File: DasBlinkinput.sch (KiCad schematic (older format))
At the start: 11 parts, among them P101 CONN_01X02, P102 CONN_01X01, P103 CONN_01X01, P104 CONN_01X05, U101 LP2980

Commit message: revised feedback resistor and updated reference voltage divider
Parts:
- removed R102: 10K, Resistors_SMD:R_0805_HandSoldering, symbol R_Small
- R102: renamed from R103; value 10K -> 5K
- RV101: value POT -> 10K; Fieldname (none) -> Value
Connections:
- net Channel1Photodetect/REF_V: now also RV101.2; no longer RV101.3
- net GND: now also RV101.1
- net at R102.1: now also RV101.3; no longer RV101.2
- no-connect marks 1 -> 0
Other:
- note added: "Note 1: Sense resistors sized for 2V @ 1uA\nNote 2: Minimum ESR required for C102\nNote 3: Input voltage is +5V\nNote 4: Reference voltage varies from 0V to +2V"
- note removed: "Note 1: Check the sense resistors\nNote 2: Spec the tantalum cap\nNote 3: Size the pot\nNote 4: Check diode current and resistor sizing"
- moved on the sheet: R102
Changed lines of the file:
@@
 $EndComp
 $Comp
-L R_Small R103
+L R_Small R102
 U 1 1 582376EF
-P 4770 4450
-F 0 "R103" V 4850 4410 50  0000 L CNN
-F 1 "10K" V 4700 4330 50  0000 L CNN
-F 2 "Resistors_SMD:R_0805_HandSoldering" H 4770 4450 50  0001 C CNN
-F 3 "" H 4770 4450 50  0000 C CNN
-F 4 "Value" H 4770 4450 60  0001 C CNN "Fieldname"
-	1    4770 4450
+P 4620 4450
+F 0 "R102" V 4700 4410 50  0000 L CNN
+F 1 "5K" V 4550 4330 50  0000 L CNN
+F 2 "Resistors_SMD:R_0805_HandSoldering" H 4620 4450 50  0001 C CNN
+F 3 "" H 4620 4450 50  0000 C CNN
+F 4 "Value" H 4620 4450 60  0001 C CNN "Fieldname"
+	1    4620 4450
 	-1   0    0    1
 $EndComp
-Text GLabel 4770 4240 1    60   Input ~ 0
+Text GLabel 4620 4240 1    60   Input ~ 0
 +3V
 $Comp
@@
 P 4620 4780
 F 0 "RV101" H 4620 4700 50  0000 C CNN
-F 1 "POT" H 4620 4780 50  0000 C CNN
+F 1 "10K" H 4620 4780 50  0000 C CNN
 F 2 "DasBlinkinput:P090L-02F25BR10K" H 4620 4780 50  0001 C CNN
 F 3 "" H 4620 4780 50  0000 C CNN
+F 4 "Value" H 4620 4780 60  0001 C CNN "Fieldname"
 	1    4620 4780
-	0    1    1    0
+	0    1    -1   0
 $EndComp
 $Comp
 L GND #PWR03
 U 1 1 582376FF
-P 4620 5320
-F 0 "#PWR03" H 4620 5070 50  0001 C CNN
-F 1 "GND" H 4620 5170 50  0000 C CNN
-F 2 "" H 4620 5320 50  0000 C CNN
-F 3 "" H 4620 5320 50  0000 C CNN
-	1    4620 5320
+P 4620 5030
+F 0 "#PWR03" H 4620 4780 50  0001 C CNN
+F 1 "GND" H 4620 4880 50  0000 C CNN
+F 2 "" H 4620 5030 50  0000 C CNN
+F 3 "" H 4620 5030 50  0000 C CNN
+	1    4620 5030
 	1    0    0    -1
-$EndComp
-NoConn ~ 4620 4630
-$Comp
-L R_Small R102
-U 1 1 58237709
-P 4620 5120
-F 0 "R102" V 4700 5080 50  0000 L CNN
-F 1 "10K" V 4550 5000 50  0000 L CNN
-F 2 "Resistors_SMD:R_0805_HandSoldering" H 4620 5120 50  0001 C CNN
-F 3 "" H 4620 5120 50  0000 C CNN
-F 4 "Value" H 4620 5120 60  0001 C CNN "Fieldname"
-	1    4620 5120
-	-1   0    0    1
 $EndComp
 Wire Wire Line
@@
 Wire Wire Line
 	970  2630 970  2880
-Wire Wire Line
-	4770 4240 4770 4350
-Wire Wire Line
-	4770 4550 4770 4780
-Wire Wire Line
-	4620 4930 4620 5020
-Wire Wire Line
-	4620 5220 4620 5320
 Wire Wire Line
 	5830 1340 6460 1340
@@
 Connection ~ 2070 3720
 Text Notes 1050 1080 0    60   ~ 0
-Note 1:  Check the sense resistors\nNote 2:  Spec the tantalum cap\nNote 3:  Size the pot\nNote 4:  Check diode current and resistor sizing
+Note 1:  Sense resistors sized for 2V @ 1uA\nNote 2:  Minimum ESR required for C102\nNote 3:  Input voltage is +5V\nNote 4:  Reference voltage varies from 0V to +2V
 Wire Wire Line
 	5830 1340 5830 5360
@@
 Connection ~ 5830 4040
 Wire Wire Line
-	4620 4970 5830 4970
-Connection ~ 5830 4970
-Connection ~ 4620 4970
+	4620 4930 4620 5030
+Wire Wire Line
+	4620 4550 4620 4630
+Wire Wire Line
+	4620 4240 4620 4350
+Wire Wire Line
+	4770 4780 5830 4780
+Connection ~ 5830 4780
 $EndSCHEMATC

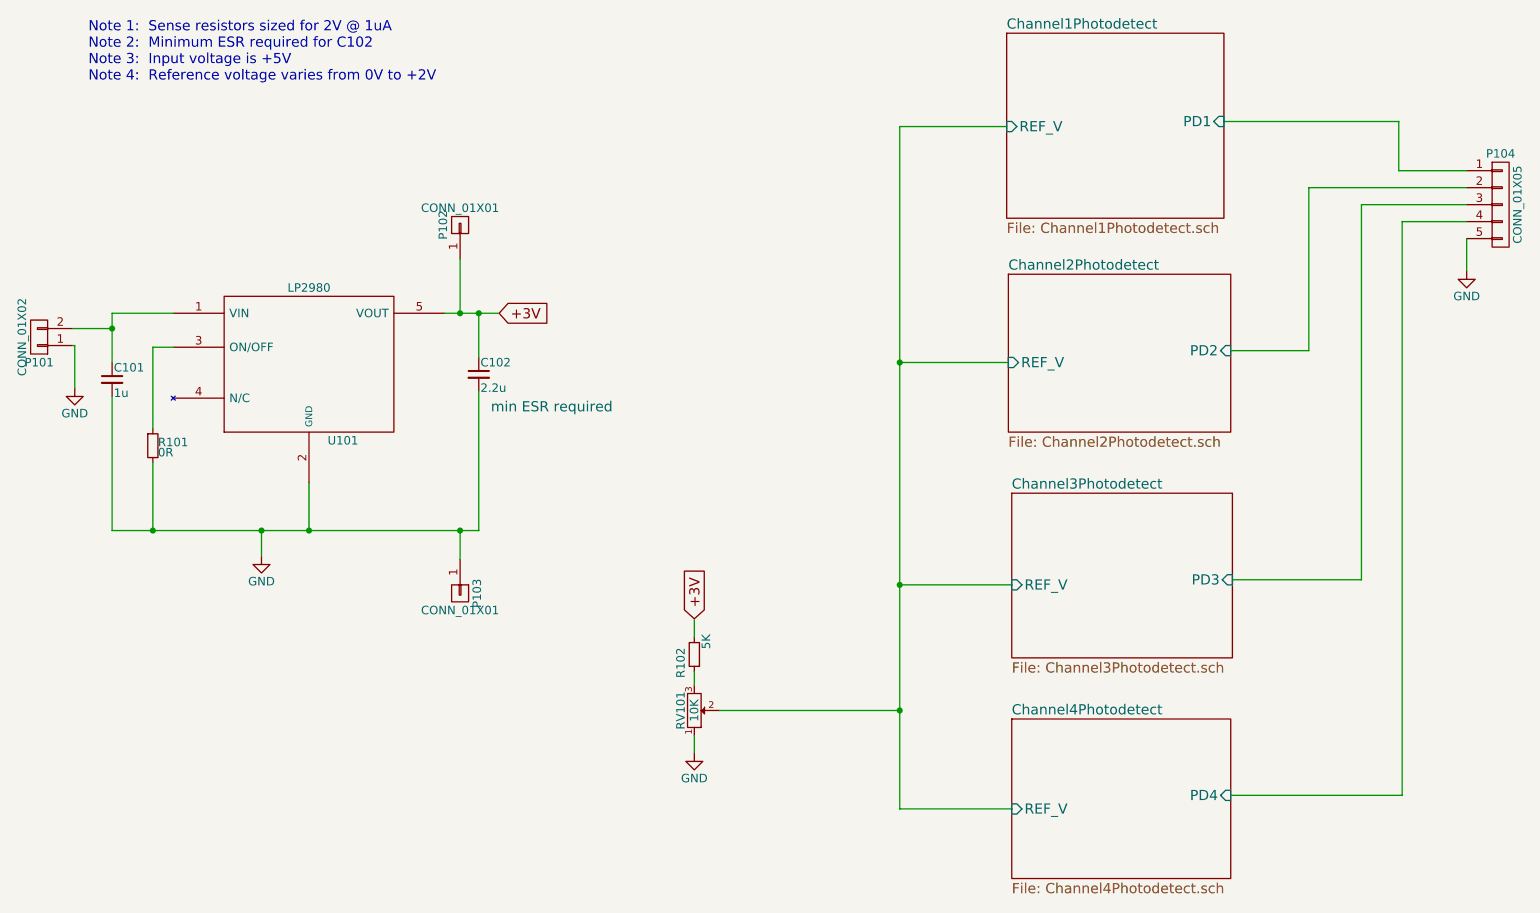
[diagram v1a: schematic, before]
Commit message: added pull-up resistors
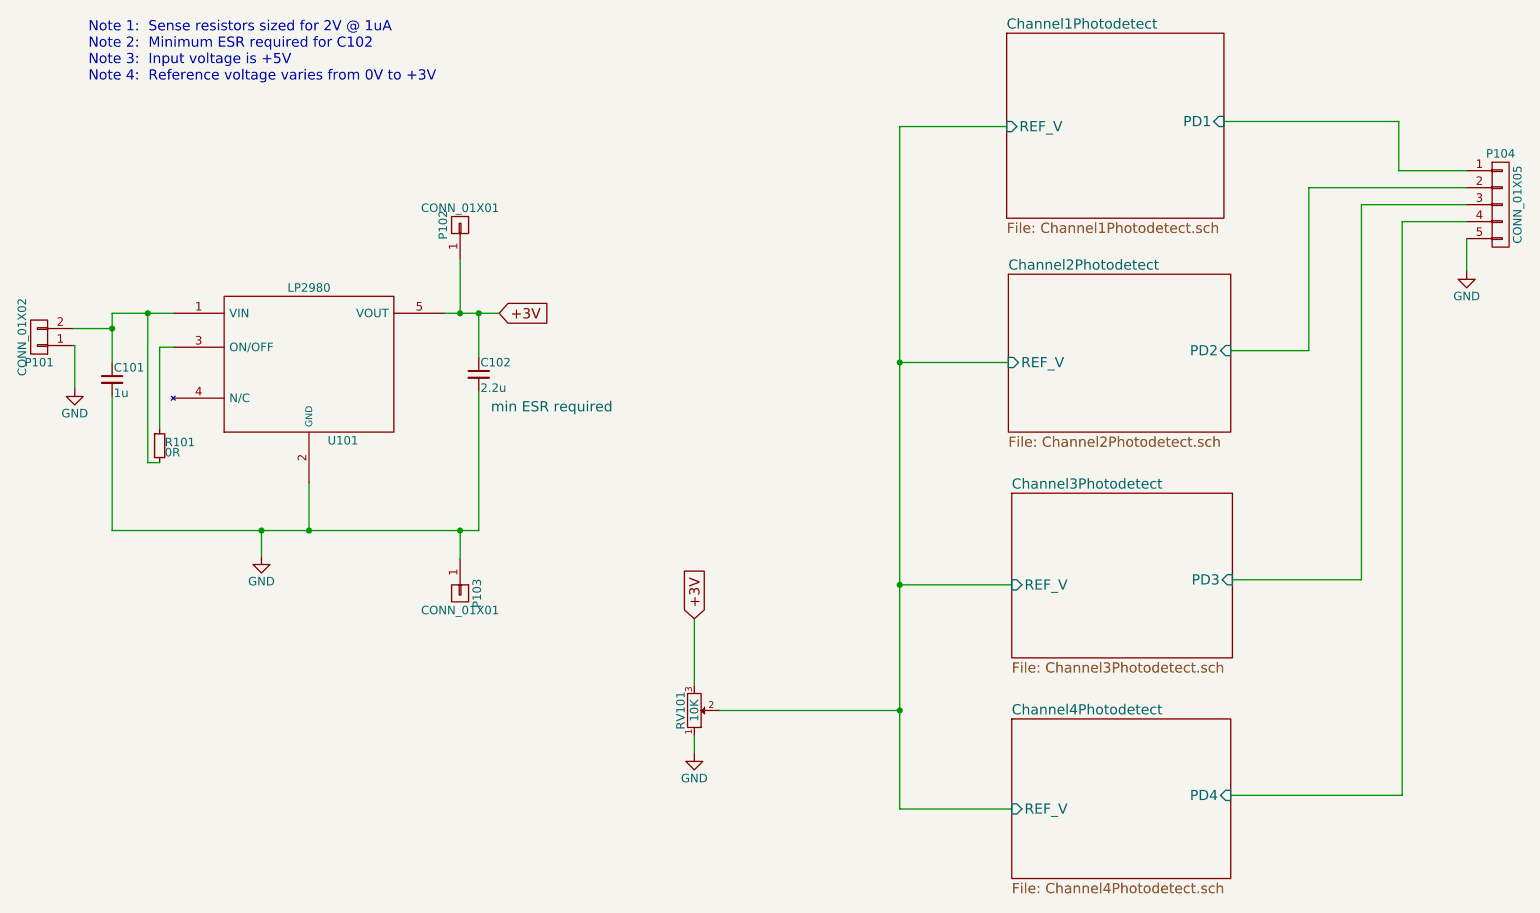
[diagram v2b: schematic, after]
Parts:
- removed R102: 5K, Resistors_SMD:R_0805_HandSoldering, symbol R_Small
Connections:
- net +3V: now also RV101.3
- net GND: no longer R101.2
- net at C101.1, P101.2 (P2), U101.1 (VIN): now also R101.2
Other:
- note added: "Note 1: Sense resistors sized for 2V @ 1uA\nNote 2: Minimum ESR required for C102\nNote 3: Input voltage is +5V\nNote 4: Reference voltage varies from 0V to +3V"
- note removed: "Note 1: Sense resistors sized for 2V @ 1uA\nNote 2: Minimum ESR required for C102\nNote 3: Input voltage is +5V\nNote 4: Reference voltage varies from 0V to +2V"
- moved on the sheet: R101
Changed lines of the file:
@@
 L R_Small R101
 U 1 1 582369B4
-P 1430 3220
-F 0 "R101" H 1460 3240 50  0000 L CNN
-F 1 "0R" H 1460 3180 50  0000 L CNN
-F 2 "Resistors_SMD:R_0805_HandSoldering" H 1430 3220 50  0001 C CNN
-F 3 "" H 1430 3220 50  0000 C CNN
-F 4 "Value" H 1430 3220 60  0001 C CNN "Fieldname"
-	1    1430 3220
+P 1470 3220
+F 0 "R101" H 1500 3240 50  0000 L CNN
+F 1 "0R" H 1500 3180 50  0000 L CNN
+F 2 "Resistors_SMD:R_0805_HandSoldering" H 1470 3220 50  0001 C CNN
+F 3 "" H 1470 3220 50  0000 C CNN
+F 4 "Value" H 1470 3220 60  0001 C CNN "Fieldname"
+	1    1470 3220
 	1    0    0    -1
 $EndComp
@@
 	1    0    0    -1
 $EndComp
-$Comp
-L R_Small R102
-U 1 1 582376EF
-P 4620 4450
-F 0 "R102" V 4700 4410 50  0000 L CNN
-F 1 "5K" V 4550 4330 50  0000 L CNN
-F 2 "Resistors_SMD:R_0805_HandSoldering" H 4620 4450 50  0001 C CNN
-F 3 "" H 4620 4450 50  0000 C CNN
-F 4 "Value" H 4620 4450 60  0001 C CNN "Fieldname"
-	1    4620 4450
-	-1   0    0    1
-$EndComp
 Text GLabel 4620 4240 1    60   Input ~ 0
 +3V
@@
 	1190 3720 1190 2930
 Wire Wire Line
-	1430 3320 1430 3720
-Connection ~ 1430 3720
-Wire Wire Line
-	1430 3120 1430 2640
-Wire Wire Line
-	1430 2640 1550 2640
-Wire Wire Line
-	1550 2440 1190 2440
+	1470 3120 1470 2640
+Wire Wire Line
+	1470 2640 1550 2640
+Wire Wire Line
+	1190 2440 1550 2440
 Wire Wire Line
 	1190 2440 1190 2730
@@
 Connection ~ 2070 3720
 Text Notes 1050 1080 0    60   ~ 0
-Note 1:  Sense resistors sized for 2V @ 1uA\nNote 2:  Minimum ESR required for C102\nNote 3:  Input voltage is +5V\nNote 4:  Reference voltage varies from 0V to +2V
+Note 1:  Sense resistors sized for 2V @ 1uA\nNote 2:  Minimum ESR required for C102\nNote 3:  Input voltage is +5V\nNote 4:  Reference voltage varies from 0V to +3V
 Wire Wire Line
 	5830 1340 5830 5360
@@
 	4620 4930 4620 5030
 Wire Wire Line
-	4620 4550 4620 4630
-Wire Wire Line
-	4620 4240 4620 4350
-Wire Wire Line
 	4770 4780 5830 4780
 Connection ~ 5830 4780
+Wire Wire Line
+	4620 4240 4620 4630
+Wire Wire Line
+	1400 3320 1470 3320
+Wire Wire Line
+	1400 3320 1400 2440
+Connection ~ 1400 2440
 $EndSCHEMATC

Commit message: replaced potentiometer with trimpot
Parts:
- RV101: footprint DasBlinkinput:P090L-02F25BR10K -> DasBlinkinput:EVM-3YSX50B14; MPN (none) -> EVM-3YSX50B14
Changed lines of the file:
@@
 F 0 "RV101" H 4620 4700 50  0000 C CNN
 F 1 "10K" H 4620 4780 50  0000 C CNN
-F 2 "DasBlinkinput:P090L-02F25BR10K" H 4620 4780 50  0001 C CNN
-F 3 "" H 4620 4780 50  0000 C CNN
-F 4 "Value" H 4620 4780 60  0001 C CNN "Fieldname"
+F 2 "DasBlinkinput:EVM-3YSX50B14" H 4620 4780 50  0001 C CNN
+F 3 "http://media.digikey.com/pdf/Data%20Sheets/Panasonic%20Resistors%20Thermistors%20PDFs/EVM-3Y_S_R_Rev2010.pdf" H 4620 4780 50  0001 C CNN
+F 4 "EVM-3YSX50B14" H 4620 4780 60  0001 C CNN "MPN"
+F 5 "Value" H 4620 4780 60  0001 C CNN "Fieldname"
 	1    4620 4780
 	0    1    -1   0
